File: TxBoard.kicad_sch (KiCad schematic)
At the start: 15 parts, among them J1 RCA Socket, Q1 RU1J002YNTCL, SW1 Pull-Up, SW2 Input(Hi-Z)/Output, SW3 High/Low

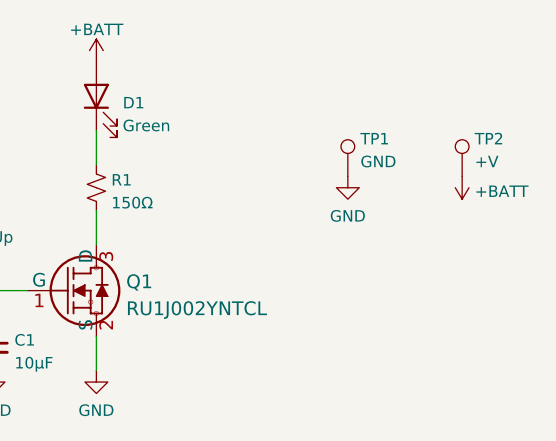
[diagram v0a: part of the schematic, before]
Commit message: Changes pre-production
License change, also
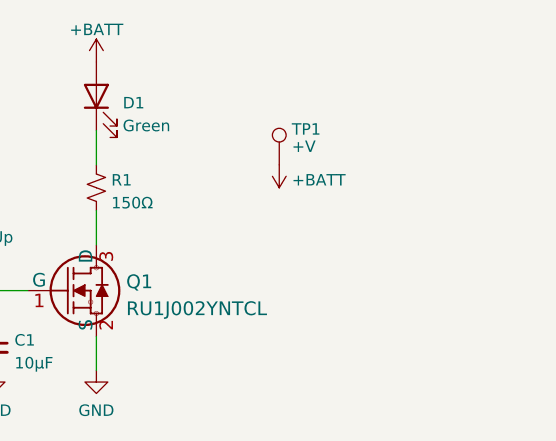
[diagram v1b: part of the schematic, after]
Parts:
- removed TP1: GND, TestPoint:TestPoint_Pad_1.5x1.5mm, symbol Connector:TestPoint
- renumbered TP2 to TP1
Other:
- moved on the sheet: TP1
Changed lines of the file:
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@@
     (comment 2 "Design Changes: Cost reduction, MOSFET changed to more suitable model with lower Vth")
     (comment 3 "Original Idea and design: https://twitter.com/m_ou_se/status/1511085846769848329")
-    (comment 4 "[Designed with <3 in San Diego - Licensed under MIT License]")
+    (comment 4 "[Designed with <3 in San Diego - CERN-OHL-P-2.0]")
   )
   (junction (at 154.94 104.14) (diameter 0) (color 0 0 0 0)
@@
     )
   )
-  (symbol (lib_id "power:GND") (at 213.36 91.44 0) (unit 1)
-    (in_bom yes) (on_board yes) (dnp no) (fields_autoplaced)
-    (property "Reference" "#PWR0110" (at 213.36 97.79 0)
-      (effects (font (size 1.27 1.27)) hide)
-    )
-    (property "Value" "GND" (at 213.36 95.8834 0)
-      (effects (font (size 1.27 1.27)))
-    )
-    (property "Footprint" "" (at 213.36 91.44 0)
-      (effects (font (size 1.27 1.27)) hide)
-    )
-    (property "Datasheet" "" (at 213.36 91.44 0)
-      (effects (font (size 1.27 1.27)) hide)
-    )
-    (pin "1")
-    (instances
-      (project "TxBoard"
-        (path "/e63e39d7-6ac0-4ffd-8aa3-1841a4541b55"
-          (reference "#PWR0110") (unit 1)
-        )
-      )
-    )
-  )
   (symbol (lib_id "power:+BATT") (at 185.42 78.74 0) (unit 1)
     (in_bom yes) (on_board yes) (dnp no) (fields_autoplaced)
@@
     )
   )
-  (symbol (lib_id "power:+BATT") (at 226.06 91.44 180) (unit 1)
-    (in_bom yes) (on_board yes) (dnp no) (fields_autoplaced)
-    (property "Reference" "#PWR0111" (at 226.06 87.63 0)
-      (effects (font (size 1.27 1.27)) hide)
-    )
-    (property "Value" "+BATT" (at 227.457 93.1438 0)
+  (symbol (lib_id "power:+BATT") (at 205.74 90.17 180) (unit 1)
+    (in_bom yes) (on_board yes) (dnp no) (fields_autoplaced)
+    (property "Reference" "#PWR0111" (at 205.74 86.36 0)
+      (effects (font (size 1.27 1.27)) hide)
+    )
+    (property "Value" "+BATT" (at 207.137 91.8738 0)
       (effects (font (size 1.27 1.27)) (justify right))
     )
-    (property "Footprint" "" (at 226.06 91.44 0)
-      (effects (font (size 1.27 1.27)) hide)
-    )
-    (property "Datasheet" "" (at 226.06 91.44 0)
+    (property "Footprint" "" (at 205.74 90.17 0)
+      (effects (font (size 1.27 1.27)) hide)
+    )
+    (property "Datasheet" "" (at 205.74 90.17 0)
       (effects (font (size 1.27 1.27)) hide)
     )
@@
     )
   )
-  (symbol (lib_id "Connector:TestPoint") (at 213.36 91.44 0) (unit 1)
-    (in_bom yes) (on_board yes) (dnp no) (fields_autoplaced)
-    (property "Reference" "TP1" (at 214.757 87.3033 0)
-      (effects (font (size 1.27 1.27)) (justify left))
-    )
-    (property "Value" "GND" (at 214.757 89.8402 0)
-      (effects (font (size 1.27 1.27)) (justify left))
-    )
-    (property "Footprint" "TestPoint:TestPoint_Pad_1.5x1.5mm" (at 218.44 91.44 0)
-      (effects (font (size 1.27 1.27)) hide)
-    )
-    (property "Datasheet" "~" (at 218.44 91.44 0)
+  (symbol (lib_id "Device:R_Small_US") (at 163.83 83.82 0) (unit 1)
+    (in_bom yes) (on_board yes) (dnp no) (fields_autoplaced)
+    (property "Reference" "R2" (at 165.481 82.9853 0)
+      (effects (font (size 1.27 1.27)) (justify left))
+    )
+    (property "Value" "22kΩ" (at 165.481 85.5222 0)
+      (effects (font (size 1.27 1.27)) (justify left))
+    )
+    (property "Footprint" "Resistor_SMD:R_0603_1608Metric" (at 163.83 83.82 0)
+      (effects (font (size 1.27 1.27)) hide)
+    )
+    (property "Datasheet" "~" (at 163.83 83.82 0)
+      (effects (font (size 1.27 1.27)) hide)
+    )
+    (pin "1")
+    (pin "2")
+    (instances
+      (project "TxBoard"
+        (path "/e63e39d7-6ac0-4ffd-8aa3-1841a4541b55"
+          (reference "R2") (unit 1)
+        )
+      )
+    )
+  )
+  (symbol (lib_id "power:GND") (at 111.76 113.03 0) (unit 1)
+    (in_bom yes) (on_board yes) (dnp no) (fields_autoplaced)
+    (property "Reference" "#PWR0112" (at 111.76 119.38 0)
+      (effects (font (size 1.27 1.27)) hide)
+    )
+    (property "Value" "GND" (at 111.76 117.4734 0)
+      (effects (font (size 1.27 1.27)))
+    )
+    (property "Footprint" "" (at 111.76 113.03 0)
+      (effects (font (size 1.27 1.27)) hide)
+    )
+    (property "Datasheet" "" (at 111.76 113.03 0)
+      (effects (font (size 1.27 1.27)) hide)
+    )
+    (pin "1")
+    (instances
+      (project "TxBoard"
+        (path "/e63e39d7-6ac0-4ffd-8aa3-1841a4541b55"
+          (reference "#PWR0112") (unit 1)
+        )
+      )
+    )
+  )
+  (symbol (lib_id "Switch:SW_SPDT") (at 149.86 97.79 0) (mirror y) (unit 1)
+    (in_bom yes) (on_board yes) (dnp no) (fields_autoplaced)
+    (property "Reference" "SW2" (at 149.86 91.1692 0)
+      (effects (font (size 1.27 1.27)))
+    )
+    (property "Value" "Input(Hi-Z)/Output" (at 149.86 93.7061 0)
+      (effects (font (size 1.27 1.27)))
+    )
+    (property "Footprint" "JS102011SCQN:JS102011SCQN" (at 149.86 97.79 0)
+      (effects (font (size 1.27 1.27)) hide)
+    )
+    (property "Datasheet" "~" (at 149.86 97.79 0)
+      (effects (font (size 1.27 1.27)) hide)
+    )
+    (pin "1")
+    (pin "2")
+    (pin "3")
+    (instances
+      (project "TxBoard"
+        (path "/e63e39d7-6ac0-4ffd-8aa3-1841a4541b55"
+          (reference "SW2") (unit 1)
+        )
+      )
+    )
+  )
+  (symbol (lib_id "Connector:TestPoint") (at 205.74 90.17 0) (unit 1)
+    (in_bom yes) (on_board yes) (dnp no) (fields_autoplaced)
+    (property "Reference" "TP1" (at 207.137 86.2243 0)
+      (effects (font (size 1.27 1.27)) (justify left))
+    )
+    (property "Value" "+V" (at 207.137 88.1453 0)
+      (effects (font (size 1.27 1.27)) (justify left))
+    )
+    (property "Footprint" "TestPoint:TestPoint_Pad_1.5x1.5mm" (at 210.82 90.17 0)
+      (effects (font (size 1.27 1.27)) hide)
+    )
+    (property "Datasheet" "~" (at 210.82 90.17 0)
       (effects (font (size 1.27 1.27)) hide)
     )
@@
         )
       )
-    )
-  )
-  (symbol (lib_id "Device:R_Small_US") (at 163.83 83.82 0) (unit 1)
-    (in_bom yes) (on_board yes) (dnp no) (fields_autoplaced)
-    (property "Reference" "R2" (at 165.481 82.9853 0)
-      (effects (font (size 1.27 1.27)) (justify left))
-    )
-    (property "Value" "22kΩ" (at 165.481 85.5222 0)
-      (effects (font (size 1.27 1.27)) (justify left))
-    )
-    (property "Footprint" "Resistor_SMD:R_0603_1608Metric" (at 163.83 83.82 0)
-      (effects (font (size 1.27 1.27)) hide)
-    )
-    (property "Datasheet" "~" (at 163.83 83.82 0)
-      (effects (font (size 1.27 1.27)) hide)
-    )
-    (pin "1")
-    (pin "2")
-    (instances
-      (project "TxBoard"
-        (path "/e63e39d7-6ac0-4ffd-8aa3-1841a4541b55"
-          (reference "R2") (unit 1)
-        )
-      )
-    )
-  )
-  (symbol (lib_id "power:GND") (at 111.76 113.03 0) (unit 1)
-    (in_bom yes) (on_board yes) (dnp no) (fields_autoplaced)
-    (property "Reference" "#PWR0112" (at 111.76 119.38 0)
-      (effects (font (size 1.27 1.27)) hide)
-    )
-    (property "Value" "GND" (at 111.76 117.4734 0)
-      (effects (font (size 1.27 1.27)))
-    )
-    (property "Footprint" "" (at 111.76 113.03 0)
-      (effects (font (size 1.27 1.27)) hide)
-    )
-    (property "Datasheet" "" (at 111.76 113.03 0)
-      (effects (font (size 1.27 1.27)) hide)
-    )
-    (pin "1")
-    (instances
-      (project "TxBoard"
-        (path "/e63e39d7-6ac0-4ffd-8aa3-1841a4541b55"
-          (reference "#PWR0112") (unit 1)
-        )
-      )
-    )
-  )
-  (symbol (lib_id "Switch:SW_SPDT") (at 149.86 97.79 0) (mirror y) (unit 1)
-    (in_bom yes) (on_board yes) (dnp no) (fields_autoplaced)
-    (property "Reference" "SW2" (at 149.86 91.1692 0)
-      (effects (font (size 1.27 1.27)))
-    )
-    (property "Value" "Input(Hi-Z)/Output" (at 149.86 93.7061 0)
-      (effects (font (size 1.27 1.27)))
-    )
-    (property "Footprint" "JS102011SCQN:JS102011SCQN" (at 149.86 97.79 0)
-      (effects (font (size 1.27 1.27)) hide)
-    )
-    (property "Datasheet" "~" (at 149.86 97.79 0)
-      (effects (font (size 1.27 1.27)) hide)
-    )
-    (pin "1")
-    (pin "2")
-    (pin "3")
-    (instances
-      (project "TxBoard"
-        (path "/e63e39d7-6ac0-4ffd-8aa3-1841a4541b55"
-          (reference "SW2") (unit 1)
-        )
-      )
-    )
-  )
-  (symbol (lib_id "Connector:TestPoint") (at 226.06 91.44 0) (unit 1)
-    (in_bom yes) (on_board yes) (dnp no) (fields_autoplaced)
-    (property "Reference" "TP2" (at 227.457 87.3033 0)
-      (effects (font (size 1.27 1.27)) (justify left))
-    )
-    (property "Value" "+V" (at 227.457 89.8402 0)
-      (effects (font (size 1.27 1.27)) (justify left))
-    )
-    (property "Footprint" "TestPoint:TestPoint_Pad_1.5x1.5mm" (at 231.14 91.44 0)
-      (effects (font (size 1.27 1.27)) hide)
-    )
-    (property "Datasheet" "~" (at 231.14 91.44 0)
-      (effects (font (size 1.27 1.27)) hide)
-    )
-    (pin "1")
-    (instances
-      (project "TxBoard"
-        (path "/e63e39d7-6ac0-4ffd-8aa3-1841a4541b55"
-          (reference "TP2") (unit 1)
-        )
-      )

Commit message: Yet more changes
Compliance and PCB and QRs, oh my!
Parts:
- BT1: footprint BC2AAPC:BAT_BC2AAPC -> TixBoard Footprints:BC2AAPC
- J1: footprint KLPX-0848A-2-B:KLPX-0848A-2-B -> TixBoard Footprints:KLPX-0848A
- SW1, SW2, SW3: footprint JS102011SCQN:JS102011SCQN -> TixBoard Footprints:JS102011SCQN
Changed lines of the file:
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@@
   (title_block
     (title "TixBoard Communications Education Board")
-    (date "2023-06-29")
+    (date "2023-06-30")
     (rev "5")
     (company "QuarterWave Engineering")
-    (comment 2 "Design Changes: Cost reduction, MOSFET changed to more suitable model with lower Vth")
     (comment 3 "Original Idea and design: https://twitter.com/m_ou_se/status/1511085846769848329")
     (comment 4 "[Designed with <3 in San Diego - CERN-OHL-P-2.0]")
@@
     (stroke (width 0) (type default))
   )
+  (text_box "Copyright QuarterWave Engineering 2023.\nThis source describes Open Hardware and is licensed under the CERN-OHL-P v2\nYou may redistribute and modify this documentation and make products\nusing it under the terms of the CERN-OHL-P v2 (https:/cern.ch/cern-ohl).\n\nThis documentation is distributed WITHOUT ANY EXPRESS OR IMPLIED\nWARRANTY, INCLUDING OF MERCHANTABILITY, SATISFACTORY QUALITY AND FITNESS FOR A PARTICULAR PURPOSE. Please see the CERN-OHL-P v2 for applicable conditions\n"
+    (at 12.7 12.7 0) (size 60.96 22.86)
+    (stroke (width 0) (type default))
+    (fill (type none))
+    (effects (font (face "Segoe UI Semibold") (size 1.27 1.27)) (justify left top))
+  )
   (symbol (lib_id "power:GND") (at 173.99 113.03 0) (unit 1)
     (in_bom yes) (on_board yes) (dnp no) (fields_autoplaced)
@@
       (effects (font (size 1.27 1.27)) (justify left))
     )
-    (property "Footprint" "KLPX-0848A-2-B:KLPX-0848A-2-B" (at 154.94 109.22 0)
-      (effects (font (size 1.27 1.27)) hide)
-    )
-    (property "Datasheet" " ~" (at 154.94 109.22 0)
+    (property "Footprint" "TixBoard Footprints:KLPX-0848A" (at 154.94 109.22 0)
+      (effects (font (size 1.27 1.27)) hide)
+    )
+    (property "Datasheet" "https://www.kycon.com/Catalog_PDF/KLPX.pdf" (at 154.94 109.22 0)
       (effects (font (size 1.27 1.27)) hide)
     )
@@
       (effects (font (size 1.27 1.27)) (justify left))
     )
-    (property "Footprint" "BC2AAPC:BAT_BC2AAPC" (at 99.06 94.996 90)
-      (effects (font (size 1.27 1.27)) hide)
-    )
-    (property "Datasheet" "~" (at 99.06 94.996 90)
+    (property "Footprint" "TixBoard Footprints:BC2AAPC" (at 99.06 94.996 90)
+      (effects (font (size 1.27 1.27)) hide)
+    )
+    (property "Datasheet" "https://media.digikey.com/pdf/Data%20Sheets/Memory%20Protection%20PDFs/BC2AAPC.pdf" (at 99.06 94.996 90)
       (effects (font (size 1.27 1.27)) hide)
     )
@@
       (effects (font (size 1.524 1.524)) hide)
     )
-    (property "Datasheet" "" (at 177.8 104.14 0)
-      (effects (font (size 1.524 1.524)))
+    (property "Datasheet" "https://fscdn.rohm.com/en/products/databook/datasheet/discrete/transistor/mosfet/ru1j002yn-e.pdf" (at 177.8 104.14 0)
+      (effects (font (size 1.524 1.524)) hide)
     )
     (property "Sim.Device" "SPICE" (at 177.8 104.14 0)
@@
       (effects (font (size 1.27 1.27)))
     )
-    (property "Footprint" "JS102011SCQN:JS102011SCQN" (at 134.62 95.25 0)
-      (effects (font (size 1.27 1.27)) hide)
-    )
-    (property "Datasheet" "~" (at 134.62 95.25 0)
+    (property "Footprint" "TixBoard Footprints:JS102011SCQN" (at 134.62 95.25 0)
+      (effects (font (size 1.27 1.27)) hide)
+    )
+    (property "Datasheet" "https://www.ckswitches.com/media/1422/js.pdf" (at 134.62 95.25 0)
       (effects (font (size 1.27 1.27)) hide)
     )
@@
       (effects (font (size 1.27 1.27)) (justify right))
     )
-    (property "Footprint" "JS102011SCQN:JS102011SCQN" (at 166.37 96.52 0)
-      (effects (font (size 1.27 1.27)) hide)
-    )
-    (property "Datasheet" "~" (at 166.37 96.52 0)
+    (property "Footprint" "TixBoard Footprints:JS102011SCQN" (at 166.37 96.52 0)
+      (effects (font (size 1.27 1.27)) hide)
+    )
+    (property "Datasheet" "https://www.ckswitches.com/media/1422/js.pdf" (at 166.37 96.52 0)
       (effects (font (size 1.27 1.27)) hide)
     )
@@
       (effects (font (size 1.27 1.27)))
     )
-    (property "Footprint" "JS102011SCQN:JS102011SCQN" (at 149.86 97.79 0)
-      (effects (font (size 1.27 1.27)) hide)
-    )
-    (property "Datasheet" "~" (at 149.86 97.79 0)
-      (effects (font (size 1.27 1.27)) hide)
-    )
+    (property "Footprint" "TixBoard Footprints:JS102011SCQN" (at 149.86 97.79 0)
+      (effects (font (size 1.27 1.27)) hide)
+    )
+    (property "Datasheet" "https://www.ckswitches.com/media/1422/js.pdf" (at 149.86 97.79 0)
+      (effects (font (size 1.27 1.27)) hide)
+    )
